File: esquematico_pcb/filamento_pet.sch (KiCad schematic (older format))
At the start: 35 parts, among them P1 Digital, P2 Analog, P3 CONN_01X01, P4 CONN_01X01, P5 CONN_01X01, P6 CONN_01X01, Q1 IRF540N, Q2 IRF540N

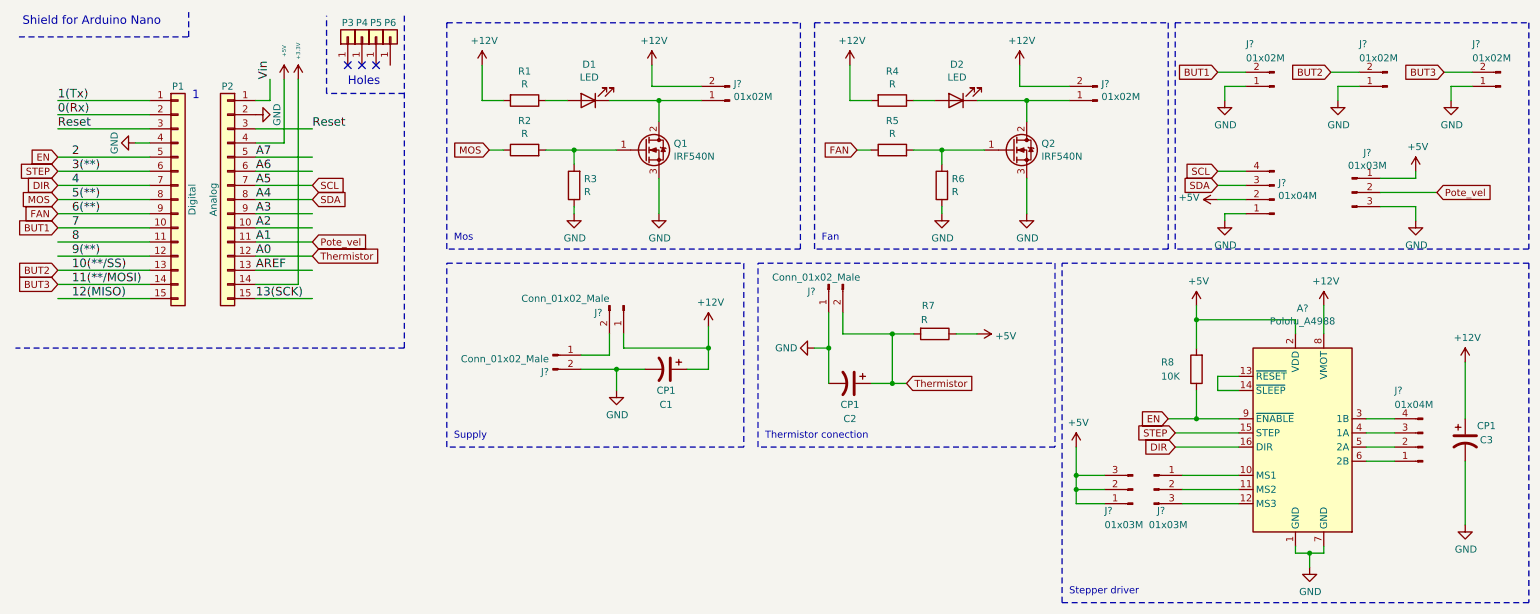
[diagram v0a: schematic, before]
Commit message: Version sin footprints, necesario para merge
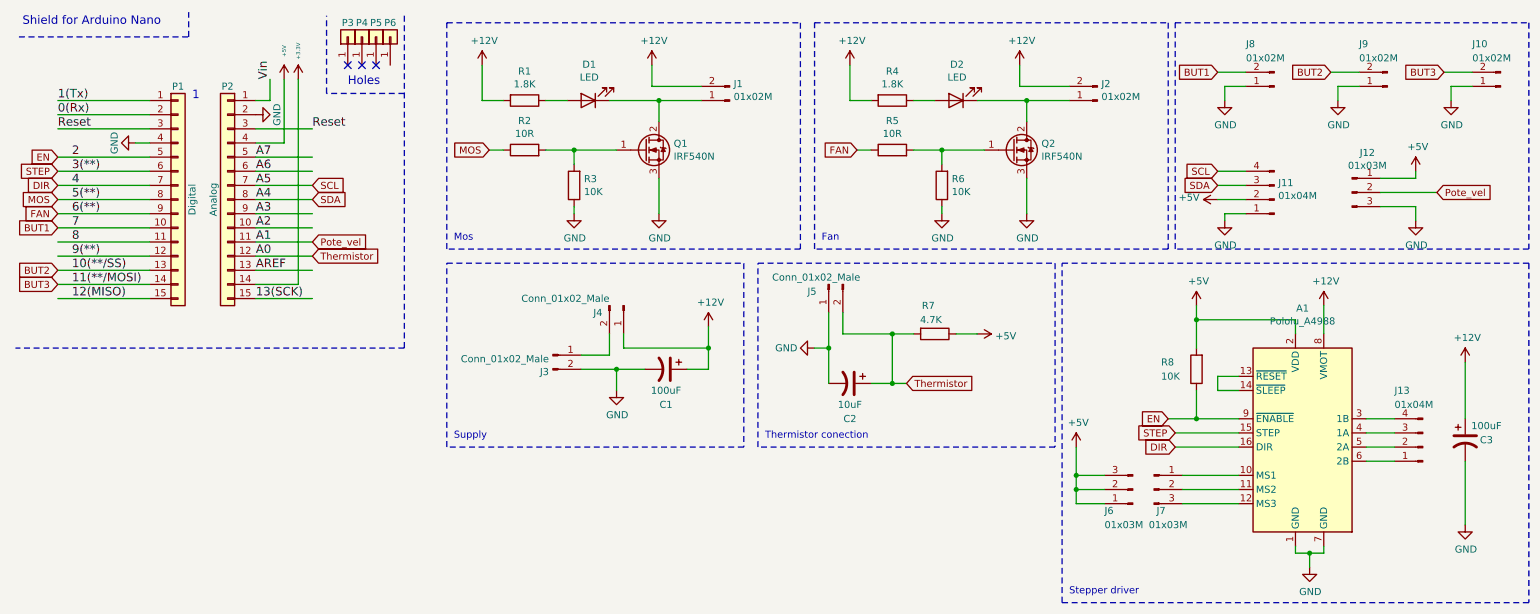
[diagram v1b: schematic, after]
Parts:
- C1, C3: value CP1 -> 100uF
- C2: value CP1 -> 10uF
- J1, J2: renamed from J?; footprint (none) -> TerminalBlock:TerminalBlock_Altech_AK300-2_P5.00mm
- J10, J8, J9: renamed from J?; footprint (none) -> Connector_PinHeader_2.54mm:PinHeader_1x02_P2.54mm_Vertical
- J11: renamed from J?; footprint (none) -> TerminalBlock:TerminalBlock_bornier-4_P5.08mm
- J12: renamed from J?; footprint (none) -> TerminalBlock:TerminalBlock_bornier-3_P5.08mm
- R1, R4: value R -> 1.8K; footprint (none) -> Resistor_THT:R_Axial_DIN0309_L9.0mm_D3.2mm_P12.70mm_Horizontal
- R2, R5: value R -> 10R; footprint (none) -> Resistor_THT:R_Axial_DIN0309_L9.0mm_D3.2mm_P12.70mm_Horizontal
- R3, R6: value R -> 10K; footprint (none) -> Resistor_THT:R_Axial_DIN0309_L9.0mm_D3.2mm_P12.70mm_Horizontal
- R7: value R -> 4.7K; footprint (none) -> Resistor_THT:R_Axial_DIN0309_L9.0mm_D3.2mm_P12.70mm_Horizontal
- R8: footprint (none) -> Resistor_THT:R_Axial_DIN0309_L9.0mm_D3.2mm_P12.70mm_Horizontal
- gave numbers to parts that had none: 7
